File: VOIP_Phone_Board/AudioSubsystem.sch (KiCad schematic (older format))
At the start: 20 parts, among them J1 69253-002LF, U1 PCM5102

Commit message: Started on the audio input section.
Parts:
- added U?: PCM1808PW, VOIP_Phone_Board:SOP65P640X120-14N, symbol PCM1808PW:PCM1808PW
- added X?: SG-8002DC, Oscillator:Oscillator_SeikoEpson_SG-8002DC, symbol Oscillator:SG-8002DC
- U1: Mouser Part Number (none) -> 595-PCM5102APW
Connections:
- net +3V3: now also X?.8 (Vcc)
- net AUDIO_MCLK: now also X?.5 (OUT)
- net GND: now also X?.4 (GND)
- net Leftout: now reaches C12.1, R5.1
- net RightOut: now reaches C10.1, R6.1
- net MIC_A(Black): now reaches J1.1
- net SPKR_A(Red): now reaches J1.2
- net SPKR_B(Green): now reaches J1.3
- net MIC_B(Yellow): now reaches J1.4
- no-connect marks 0 -> 1
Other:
- moved on the sheet: J1
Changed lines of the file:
@@
 F 2 "Package_SO:TSSOP-20_4.4x6.5mm_P0.65mm" H 3100 3400 50  0001 C CNN
 F 3 "http://www.ti.com/lit/ds/symlink/pcm5102.pdf" H 3100 3400 50  0001 C CNN
+F 4 "595-PCM5102APW" H 3150 2650 50  0001 C CNN "Mouser Part Number"
 	1    3150 2650
 	1    0    0    -1
@@
 	2150 2450 1850 2450
 Wire Wire Line
-	2150 2550 1850 2550
+	2150 2550 1950 2550
 Wire Wire Line
 	2650 3050 2400 3050
@@
 L 69253-002LF:69253-002LF J1
 U 1 1 6256F547
-P 9650 2700
-F 0 "J1" H 10050 2965 50  0000 C CNN
-F 1 "69253-002LF" H 10050 2874 50  0000 C CNN
-F 2 "VOIP_Phone_Board:69253002LF" H 10300 2800 50  0001 L CNN
-F 3 "https://www.amphenol-icc.com/media/wysiwyg/files/drawing/69253.pdf" H 10300 2700 50  0001 L CNN
-F 4 "Modular Connectors / Ethernet Connectors 4POS/1PORT CAT 3 VERTICAL" H 10300 2600 50  0001 L CNN "Description"
-F 5 "15.77" H 10300 2500 50  0001 L CNN "Height"
-F 6 "649-69253-002LF" H 10300 2400 50  0001 L CNN "Mouser Part Number"
-F 7 "https://www.mouser.co.uk/ProductDetail/Amphenol-FCI/69253-002LF?qs=6FviONYszHchXJMjMf3GPg%3D%3D" H 10300 2300 50  0001 L CNN "Mouser Price/Stock"
-F 8 "Amphenol" H 10300 2200 50  0001 L CNN "Manufacturer_Name"
-F 9 "69253-002LF" H 10300 2100 50  0001 L CNN "Manufacturer_Part_Number"
-	1    9650 2700
-	1    0    0    -1
-$EndComp
+P 8600 2350
+F 0 "J1" H 9000 2615 50  0000 C CNN
+F 1 "69253-002LF" H 9000 2524 50  0000 C CNN
+F 2 "VOIP_Phone_Board:69253002LF" H 9250 2450 50  0001 L CNN
+F 3 "https://www.amphenol-icc.com/media/wysiwyg/files/drawing/69253.pdf" H 9250 2350 50  0001 L CNN
+F 4 "Modular Connectors / Ethernet Connectors 4POS/1PORT CAT 3 VERTICAL" H 9250 2250 50  0001 L CNN "Description"
+F 5 "15.77" H 9250 2150 50  0001 L CNN "Height"
+F 6 "649-69253-002LF" H 9250 2050 50  0001 L CNN "Mouser Part Number"
+F 7 "https://www.mouser.co.uk/ProductDetail/Amphenol-FCI/69253-002LF?qs=6FviONYszHchXJMjMf3GPg%3D%3D" H 9250 1950 50  0001 L CNN "Mouser Price/Stock"
+F 8 "Amphenol" H 9250 1850 50  0001 L CNN "Manufacturer_Name"
+F 9 "69253-002LF" H 9250 1750 50  0001 L CNN "Manufacturer_Part_Number"
+	1    8600 2350
+	1    0    0    -1
+$EndComp
+$Comp
+L Oscillator:SG-8002DC X?
+U 1 1 6258A801
+P 3250 4500
+F 0 "X?" H 2906 4546 50  0000 R CNN
+F 1 "SG-8002DC" H 2906 4455 50  0000 R CNN
+F 2 "Oscillator:Oscillator_SeikoEpson_SG-8002DC" H 3700 4150 50  0001 C CNN
+F 3 "https://support.epson.biz/td/api/doc_check.php?mode=dl&lang=en&Parts=SG-8002DC" H 3150 4500 50  0001 C CNN
+F 4 "732-SG-8002DC6.144R" H 3250 4500 50  0001 C CNN "Mouser Part Number"
+	1    3250 4500
+	-1   0    0    -1
+$EndComp
+Wire Wire Line
+	2950 4500 1950 4500
+Wire Wire Line
+	1950 4500 1950 2550
+Connection ~ 1950 2550
+Wire Wire Line
+	1950 2550 1850 2550
+$Comp
+L power:+3.3V #PWR?
+U 1 1 6258D174
+P 3250 4100
+F 0 "#PWR?" H 3250 3950 50  0001 C CNN
+F 1 "+3.3V" H 3265 4273 50  0000 C CNN
+F 2 "" H 3250 4100 50  0001 C CNN
+F 3 "" H 3250 4100 50  0001 C CNN
+	1    3250 4100
+	1    0    0    -1
+$EndComp
+$Comp
+L power:GND #PWR?
+U 1 1 6258D7D4
+P 3250 5000
+F 0 "#PWR?" H 3250 4750 50  0001 C CNN
+F 1 "GND" H 3255 4827 50  0000 C CNN
+F 2 "" H 3250 5000 50  0001 C CNN
+F 3 "" H 3250 5000 50  0001 C CNN
+	1    3250 5000
+	1    0    0    -1
+$EndComp
+NoConn ~ 3550 4500
+Wire Wire Line
+	3250 4100 3250 4200
+Wire Wire Line
+	3250 4800 3250 5000
+$Comp
+L PCM1808PW:PCM1808PW U?
+U 1 1 62597D3A
+P 2750 5750
+F 0 "U?" H 3300 6015 50  0000 C CNN
+F 1 "PCM1808PW" H 3300 5924 50  0000 C CNN
+F 2 "VOIP_Phone_Board:SOP65P640X120-14N" H 3700 5850 50  0001 L CNN
+F 3 "http://www.ti.com/lit/gpn/pcm1808" H 3700 5750 50  0001 L CNN
+F 4 "99dB SNR Stereo ADC With Single-Ended Inputs" H 3700 5650 50  0001 L CNN "Description"
+F 5 "1.2" H 3700 5550 50  0001 L CNN "Height"
+F 6 "595-PCM1808PW" H 3700 5450 50  0001 L CNN "Mouser Part Number"
+F 7 "https://www.mouser.co.uk/ProductDetail/Texas-Instruments/PCM1808PW?qs=iSMark9AYDWYQaMpH%2FhwPg%3D%3D" H 3700 5350 50  0001 L CNN "Mouser Price/Stock"
+F 8 "Texas Instruments" H 3700 5250 50  0001 L CNN "Manufacturer_Name"
+F 9 "PCM1808PW" H 3700 5150 50  0001 L CNN "Manufacturer_Part_Number"
+	1    2750 5750
+	1    0    0    -1
+$EndComp
+Text Label 4800 2250 0    50   ~ 0
+Leftout
+Text Label 4350 2350 0    50   ~ 0
+RightOut
+Text Label 2050 2250 2    50   ~ 0
+DAP4_FS
+Text Label 8600 2350 2    50   ~ 0
+MIC_A(Black)
+Text Label 8600 2450 2    50   ~ 0
+SPKR_B(Green)
+Text Label 9400 2350 0    50   ~ 0
+SPKR_A(Red)
+Text Label 9400 2450 0    50   ~ 0
+MIC_B(Yellow)
 $EndSCHEMATC

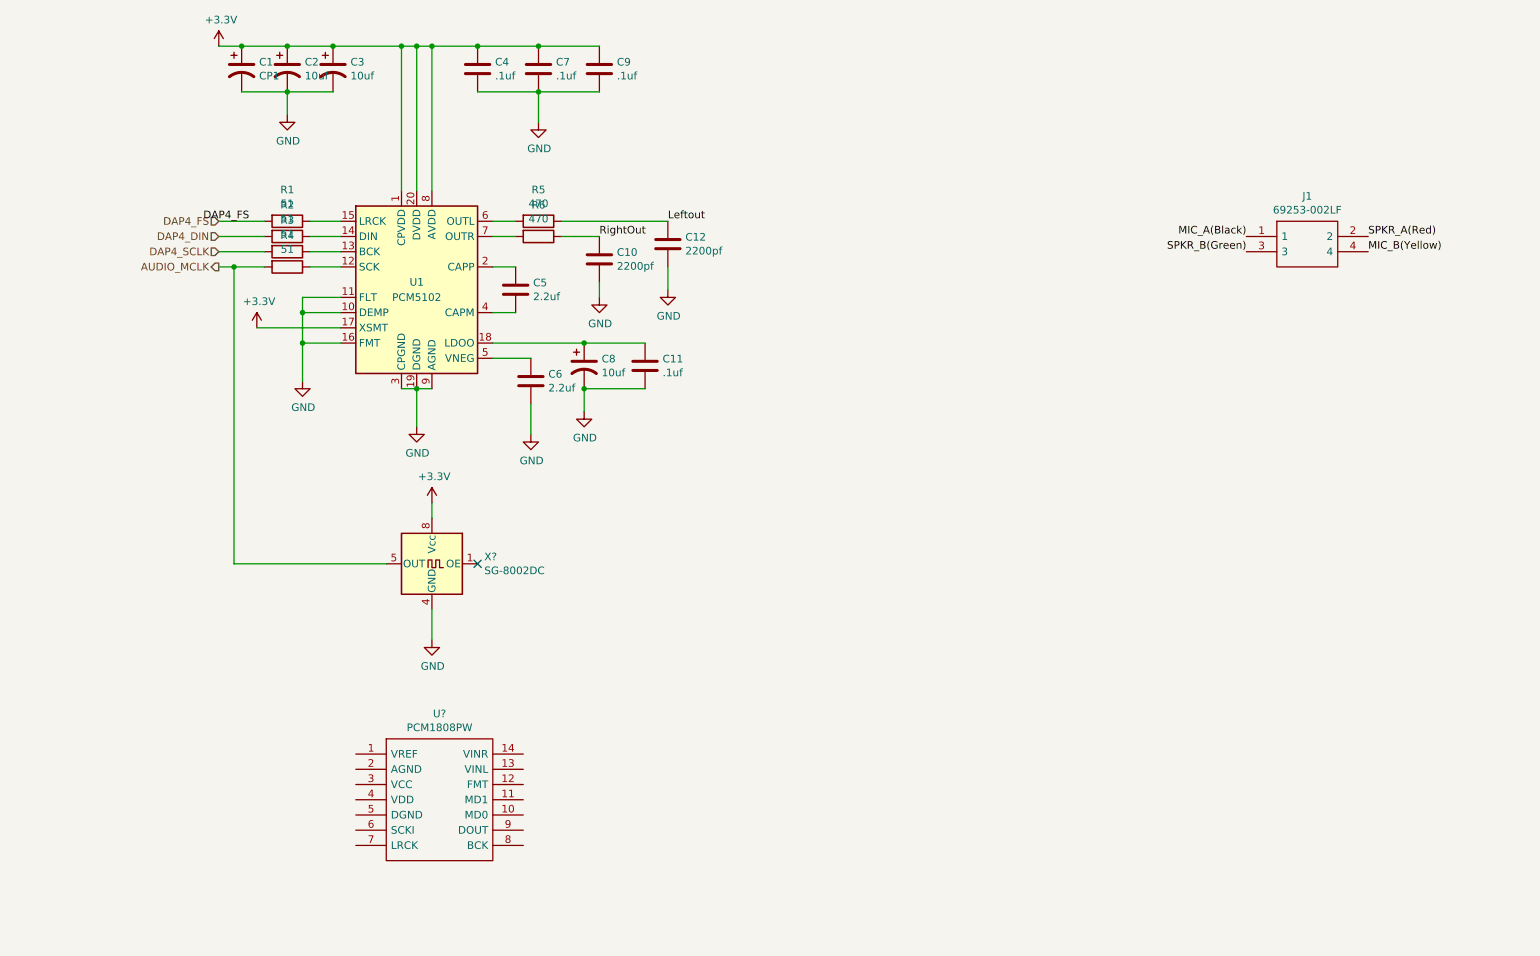
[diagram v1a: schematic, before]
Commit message: Completed audio input section.
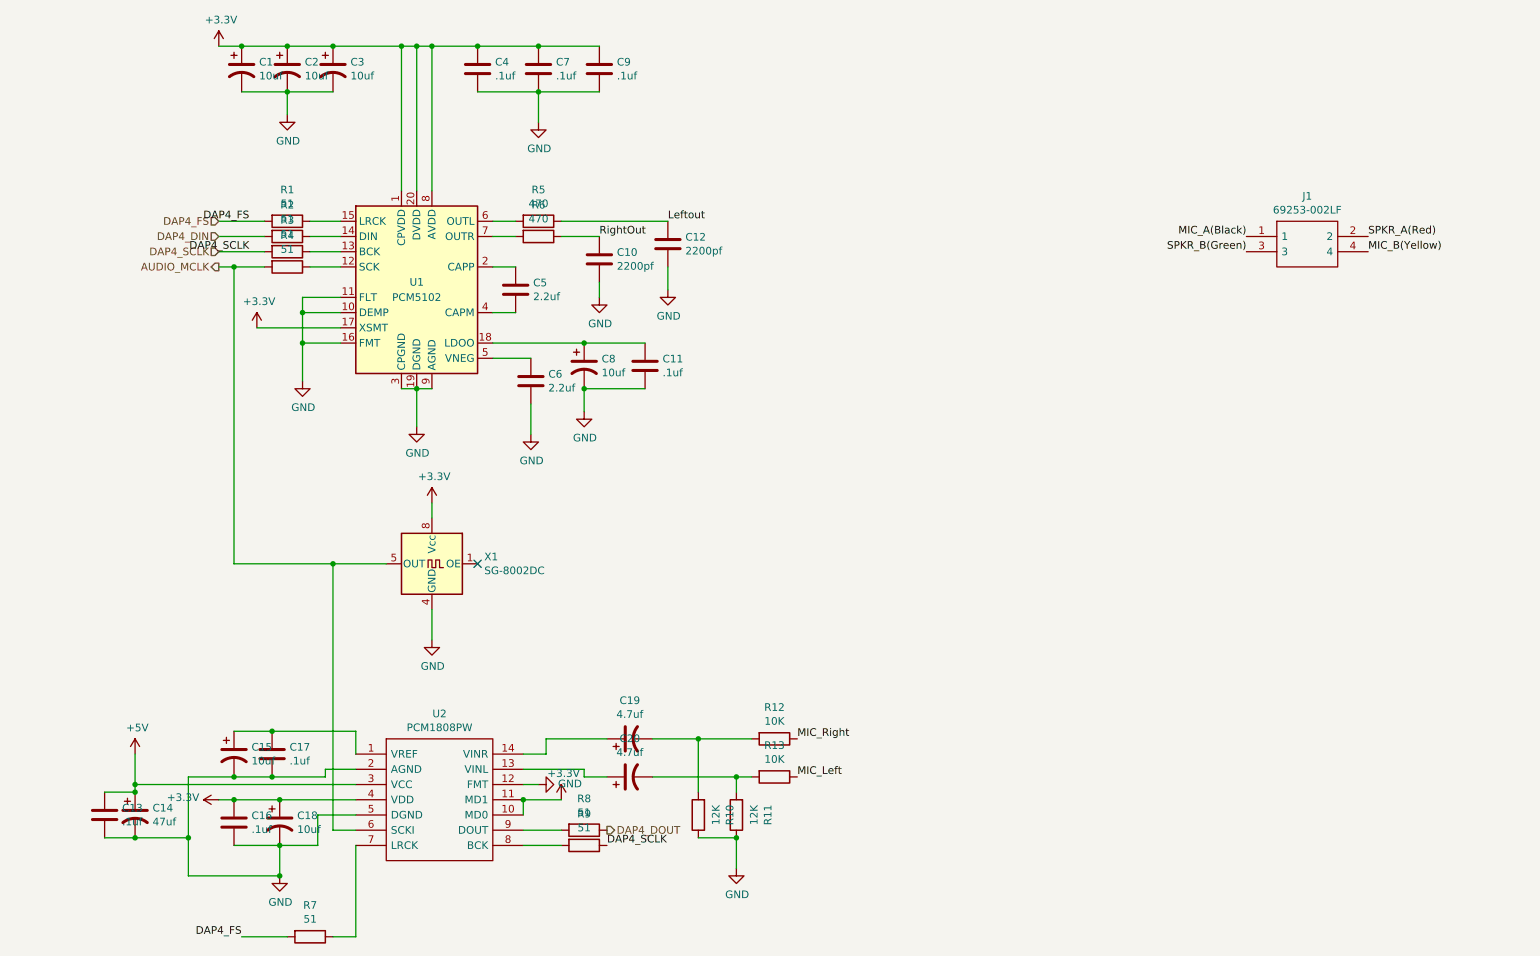
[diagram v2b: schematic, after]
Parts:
- added C13, C16, C17: .1uf, Capacitor_SMD:C_0603_1608Metric_Pad1.05x0.95mm_HandSolder, symbol Device:C
- added C14: 47uf, Capacitor_THT:CP_Radial_D6.3mm_P2.50mm, symbol Device:CP1
- added C15, C18: 10uf, VOIP_Phone_Board:CP_0603_1608Metric_Pad1.05x0.95mm_HandSolder, symbol Device:CP1
- added C19, C20: 4.7uf, VOIP_Phone_Board:CP_0603_1608Metric_Pad1.05x0.95mm_HandSolder, symbol Device:CP1
- added R10, R11: 12K, Resistor_SMD:R_0603_1608Metric_Pad1.05x0.95mm_HandSolder, symbol Device:R
- added R12, R13: 10K, Resistor_SMD:R_0603_1608Metric_Pad1.05x0.95mm_HandSolder, symbol Device:R
- added R7, R8, R9: 51, Resistor_SMD:R_0603_1608Metric_Pad1.05x0.95mm_HandSolder, symbol Device:R
- C1: value CP1 -> 10uf
- gave numbers to parts that had none: 2
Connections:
- net +3V3: now also U2.10 (MD0), U2.11 (MD1), U2.4 (VDD), C16.1, C18.1
- net AUDIO_MCLK: now also U2.6 (SCKI)
- net DAP4_FS: now also R7.2
- net DAP4_SCLK: now also R9.1
- net GND: now also U2.12 (FMT), U2.2 (AGND), U2.5 (DGND), C13.2, C14.2, C15.2, C16.2, C17.2, C18.2, R10.1, R11.1
- net at U2.1 (VREF): now also C15.1, C17.1
- net at U2.13 (VINL): now also C20.1
- net at U2.14 (VINR): now also C19.1
- net +5V: now reaches U2.3 (VCC)
- net +5V: now also C13.1, C14.1
- net at U2.7 (LRCK): now also R7.1
- net at U2.8 (BCK): now also R9.2
- net at U2.9 (DOUT): now also R8.2
- new net: C19.2, R10.2, R12.2
- new net: C20.2, R11.2, R13.2
- new net DAP4_DOUT: R8.1
- new net MIC_Left: R13.1
- new net MIC_Right: R12.1

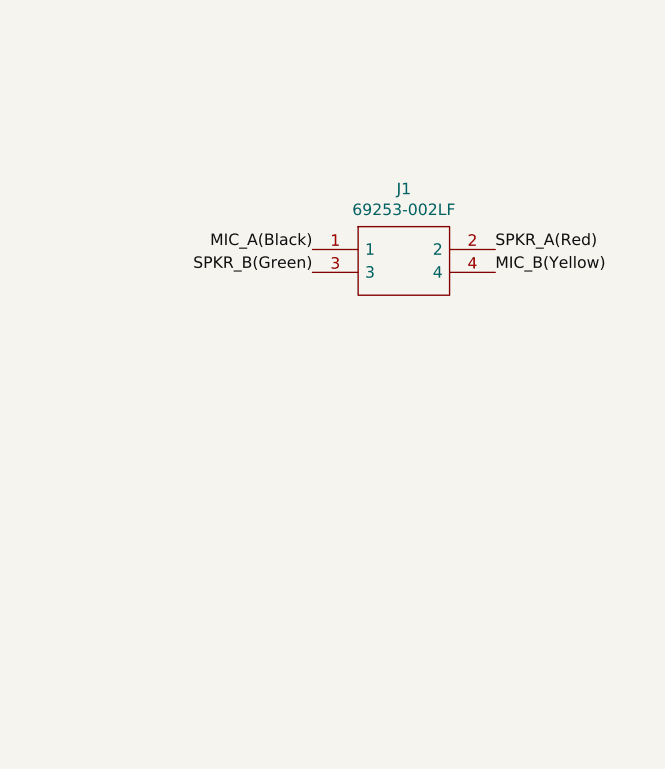
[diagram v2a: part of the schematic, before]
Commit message: Complete all I/O and connectors.
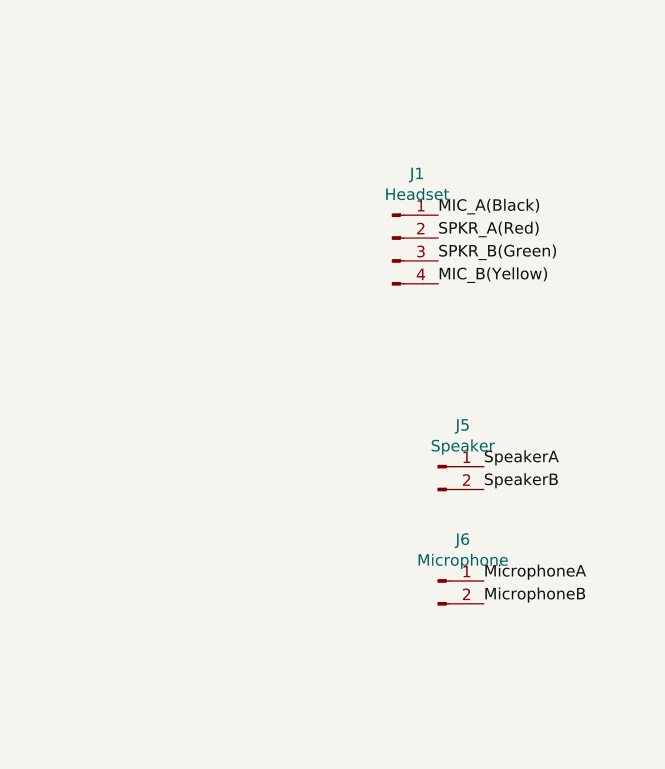
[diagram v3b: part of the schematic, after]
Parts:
- removed J1: 69253-002LF, VOIP_Phone_Board:69253002LF, symbol 69253-002LF:69253-002LF
- added J1: Headset, Connector_PinHeader_2.54mm:PinHeader_1x04_P2.54mm_Vertical, symbol Connector:Conn_01x04_Male
- added J5: Speaker, Connector_PinHeader_2.54mm:PinHeader_1x02_P2.54mm_Vertical, symbol Connector:Conn_01x02_Male
- added J6: Microphone, Connector_PinHeader_2.54mm:PinHeader_1x02_P2.54mm_Vertical, symbol Connector:Conn_01x02_Male
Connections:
- net MIC_A(Black): now also J1.1 (Pin_1)
- net MIC_B(Yellow): now also J1.4 (Pin_4)
- net SPKR_A(Red): now also J1.2 (Pin_2)
- net SPKR_B(Green): now also J1.3 (Pin_3)
- new net MicrophoneA: J6.1 (Pin_1)
- new net MicrophoneB: J6.2 (Pin_2)
- new net SpeakerA: J5.1 (Pin_1)
- new net SpeakerB: J5.2 (Pin_2)
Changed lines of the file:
@@
 $Descr A4 11693 8268
 encoding utf-8
-Sheet 2 4
+Sheet 2 2
 Title ""
 Date ""
@@
 Wire Wire Line
 	2400 2850 2400 2750
-$Comp
-L 69253-002LF:69253-002LF J1
-U 1 1 6256F547
-P 8600 2350
-F 0 "J1" H 9000 2615 50  0000 C CNN
-F 1 "69253-002LF" H 9000 2524 50  0000 C CNN
-F 2 "VOIP_Phone_Board:69253002LF" H 9250 2450 50  0001 L CNN
-F 3 "https://www.amphenol-icc.com/media/wysiwyg/files/drawing/69253.pdf" H 9250 2350 50  0001 L CNN
-F 4 "Modular Connectors / Ethernet Connectors 4POS/1PORT CAT 3 VERTICAL" H 9250 2250 50  0001 L CNN "Description"
-F 5 "15.77" H 9250 2150 50  0001 L CNN "Height"
-F 6 "649-69253-002LF" H 9250 2050 50  0001 L CNN "Mouser Part Number"
-F 7 "https://www.mouser.co.uk/ProductDetail/Amphenol-FCI/69253-002LF?qs=6FviONYszHchXJMjMf3GPg%3D%3D" H 9250 1950 50  0001 L CNN "Mouser Price/Stock"
-F 8 "Amphenol" H 9250 1850 50  0001 L CNN "Manufacturer_Name"
-F 9 "69253-002LF" H 9250 1750 50  0001 L CNN "Manufacturer_Part_Number"
-	1    8600 2350
-	1    0    0    -1
-$EndComp
 $Comp
 L Oscillator:SG-8002DC X1
@@
 Text Label 2050 2250 2    50   ~ 0
 DAP4_FS
-Text Label 8600 2350 2    50   ~ 0
+Text Label 9150 2200 0    50   ~ 0
 MIC_A(Black)
-Text Label 8600 2450 2    50   ~ 0
+Text Label 9150 2400 0    50   ~ 0
 SPKR_B(Green)
-Text Label 9400 2350 0    50   ~ 0
+Text Label 9150 2300 0    50   ~ 0
 SPKR_A(Red)
-Text Label 9400 2450 0    50   ~ 0
+Text Label 9150 2500 0    50   ~ 0
 MIC_B(Yellow)
 $Comp
@@
 Text Label 5650 5650 0    50   ~ 0
 MIC_Right
+$Comp
+L Connector:Conn_01x04_Male J1
+U 1 1 6261E09C
+P 8950 2300
+F 0 "J1" H 9058 2581 50  0000 C CNN
+F 1 "Headset" H 9058 2490 50  0000 C CNN
+F 2 "Connector_PinHeader_2.54mm:PinHeader_1x04_P2.54mm_Vertical" H 8950 2300 50  0001 C CNN
+F 3 "~" H 8950 2300 50  0001 C CNN
+	1    8950 2300
+	1    0    0    -1
+$EndComp
+$Comp
+L Connector:Conn_01x02_Male J5
+U 1 1 6254E63A
+P 9150 3300
+F 0 "J5" H 9258 3481 50  0000 C CNN
+F 1 "Speaker" H 9258 3390 50  0000 C CNN
+F 2 "Connector_PinHeader_2.54mm:PinHeader_1x02_P2.54mm_Vertical" H 9150 3300 50  0001 C CNN
+F 3 "~" H 9150 3300 50  0001 C CNN
+	1    9150 3300
+	1    0    0    -1
+$EndComp
+$Comp
+L Connector:Conn_01x02_Male J6
+U 1 1 6254EECA
+P 9150 3800
+F 0 "J6" H 9258 3981 50  0000 C CNN
+F 1 "Microphone" H 9258 3890 50  0000 C CNN
+F 2 "Connector_PinHeader_2.54mm:PinHeader_1x02_P2.54mm_Vertical" H 9150 3800 50  0001 C CNN
+F 3 "~" H 9150 3800 50  0001 C CNN
+	1    9150 3800
+	1    0    0    -1
+$EndComp
+Text Label 9350 3300 0    50   ~ 0
+SpeakerA
+Text Label 9350 3400 0    50   ~ 0
+SpeakerB
+Text Label 9350 3800 0    50   ~ 0
+MicrophoneA
+Text Label 9350 3900 0    50   ~ 0
+MicrophoneB
 $EndSCHEMATC
